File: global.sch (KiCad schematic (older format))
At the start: 37 parts, among them Q5 MMBT3904, U11 74HC165, U12 74HC595, U13 74HC595, U14 74HC595, U5 74HCT125

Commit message: added package field
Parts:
- C44, C45, C46, C50, C6, R10, R11, R34, R47, R48, R53, R56, R59, R64, R65, R67, R68, R69, R7, R70, R71, R72, R73, R74, R75, R8, R9: Package (none) -> 0603
- Q5: Package (none) -> SOT-23
- U11, U12, U13, U14: Package (none) -> SOIC-16
- U5: Package (none) -> SOIC-14
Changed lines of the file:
@@
 F 4 "Texas Instruments" H 6000 4350 50  0001 C CNN "MFN"
 F 5 "SN74HC165D" H 6000 4350 50  0001 C CNN "MFP"
+F 6 "SOIC-16" H 6000 4350 50  0001 C CNN "Package"
 	1    5500 5100
 	1    0    0    -1
@@
 F 4 "Texas Instruments" H 6000 150 50  0001 C CNN "MFN"
 F 5 "SN74HC595D" H 6000 150 50  0001 C CNN "MFP"
+F 6 "SOIC-16" H 6000 150 50  0001 C CNN "Package"
 	1    5500 900
 	1    0    0    -1
@@
 F 4 "Texas Instruments" H 6000 1550 50  0001 C CNN "MFN"
 F 5 "SN74HC595D" H 6000 1550 50  0001 C CNN "MFP"
+F 6 "SOIC-16" H 5500 2300 60  0001 C CNN "Package"
 	1    5500 2300
 	1    0    0    -1
@@
 F 4 "Texas Instruments" H 6000 2950 50  0001 C CNN "MFN"
 F 5 "SN74HC595D" H 6000 2950 50  0001 C CNN "MFP"
+F 6 "SOIC-16" H 6000 2950 50  0001 C CNN "Package"
 	1    5500 3700
 	1    0    0    -1
@@
 F 4 "Murata" H 5025 7050 50  0001 C CNN "MFN"
 F 5 "GRM188R71E104JA01J" H 5025 7050 50  0001 C CNN "MFP"
+F 6 "0603" H 5025 7050 50  0001 C CNN "Package"
 	1    5000 6850
 	1    0    0    -1
@@
 F 4 "Murata" H 5325 7050 50  0001 C CNN "MFN"
 F 5 "GRM188R71E104JA01J" H 5325 7050 50  0001 C CNN "MFP"
+F 6 "0603" H 5325 7050 50  0001 C CNN "Package"
 	1    5300 6850
 	1    0    0    -1
@@
 F 4 "Murata" H 5625 7050 50  0001 C CNN "MFN"
 F 5 "GRM188R71E104JA01J" H 5625 7050 50  0001 C CNN "MFP"
+F 6 "0603" H 5625 7050 50  0001 C CNN "Package"
 	1    5600 6850
 	1    0    0    -1
@@
 F 4 "Murata" H 5925 7050 50  0001 C CNN "MFN"
 F 5 "GRM188R71E104JA01J" H 5925 7050 50  0001 C CNN "MFP"
+F 6 "0603" H 5925 7050 50  0001 C CNN "Package"
 	1    5900 6850
 	1    0    0    -1
@@
 F 4 "Murata" H 6225 7050 50  0001 C CNN "MFN"
 F 5 "GRM188R71E104JA01J" H 6225 7050 50  0001 C CNN "MFP"
+F 6 "0603" H 6225 7050 50  0001 C CNN "Package"
 	1    6200 6850
 	1    0    0    -1
@@
 F 4 "Panasonic" H 6650 5200 50  0001 C CNN "MFN"
 F 5 "ERJ-3EKF1002V" H 6650 5200 50  0001 C CNN "MFP"
+F 6 "0603" H 6650 5200 50  0001 C CNN "Package"
 	1    6700 4950
 	1    0    0    -1
@@
 F 4 "Panasonic" H 6750 5200 50  0001 C CNN "MFN"
 F 5 "ERJ-3EKF1002V" H 6750 5200 50  0001 C CNN "MFP"
+F 6 "0603" H 6750 5200 50  0001 C CNN "Package"
 	1    6800 4950
 	1    0    0    -1
@@
 F 4 "Panasonic" H 6850 5200 50  0001 C CNN "MFN"
 F 5 "ERJ-3EKF1002V" H 6850 5200 50  0001 C CNN "MFP"
+F 6 "0603" H 6850 5200 50  0001 C CNN "Package"
 	1    6900 4950
 	1    0    0    -1
@@
 F 4 "Panasonic" H 6950 5200 50  0001 C CNN "MFN"
 F 5 "ERJ-3EKF1002V" H 6950 5200 50  0001 C CNN "MFP"
+F 6 "0603" H 6950 5200 50  0001 C CNN "Package"
 	1    7000 4950
 	1    0    0    -1
@@
 F 4 "Panasonic" H 7050 5200 50  0001 C CNN "MFN"
 F 5 "ERJ-3EKF1002V" H 7050 5200 50  0001 C CNN "MFP"
+F 6 "0603" H 7050 5200 50  0001 C CNN "Package"
 	1    7100 4950
 	1    0    0    -1
@@
 F 4 "Panasonic" H 6700 2650 50  0001 C CNN "MFN"
 F 5 "ERJ-3EKF1001V" H 6700 2650 50  0001 C CNN "MFP"
+F 6 "0603" H 6700 2650 50  0001 C CNN "Package"
 	1    6750 2400
 	0    1    1    0
@@
 F 4 "Panasonic" H 6700 2550 50  0001 C CNN "MFN"
 F 5 "ERJ-3EKF1001V" H 6700 2550 50  0001 C CNN "MFP"
+F 6 "0603" H 6700 2550 50  0001 C CNN "Package"
 	1    6750 2300
 	0    1    1    0
@@
 F 4 "Panasonic" H 6700 2750 50  0001 C CNN "MFN"
 F 5 "ERJ-3EKF1001V" H 6700 2750 50  0001 C CNN "MFP"
+F 6 "0603" H 6700 2750 50  0001 C CNN "Package"
 	1    6750 2500
 	0    1    1    0
@@
 F 4 "Panasonic" H 6700 2850 50  0001 C CNN "MFN"
 F 5 "ERJ-3EKF1001V" H 6700 2850 50  0001 C CNN "MFP"
+F 6 "0603" H 6700 2850 50  0001 C CNN "Package"
 	1    6750 2600
 	0    1    1    0
@@
 F 4 "Panasonic" H 6700 3250 50  0001 C CNN "MFN"
 F 5 "ERJ-3EKF1001V" H 6700 3250 50  0001 C CNN "MFP"
+F 6 "0603" H 6700 3250 50  0001 C CNN "Package"
 	1    6750 3000
 	0    1    1    0
@@
 F 4 "Panasonic" H 6700 3150 50  0001 C CNN "MFN"
 F 5 "ERJ-3EKF1001V" H 6700 3150 50  0001 C CNN "MFP"
+F 6 "0603" H 6700 3150 50  0001 C CNN "Package"
 	1    6750 2900
 	0    1    1    0
@@
 F 4 "Panasonic" H 6700 3050 50  0001 C CNN "MFN"
 F 5 "ERJ-3EKF1001V" H 6700 3050 50  0001 C CNN "MFP"
+F 6 "0603" H 6700 3050 50  0001 C CNN "Package"
 	1    6750 2800
 	0    1    1    0
@@
 F 4 "Panasonic" H 6700 2950 50  0001 C CNN "MFN"
 F 5 "ERJ-3EKF1001V" H 6700 2950 50  0001 C CNN "MFP"
+F 6 "0603" H 6700 2950 50  0001 C CNN "Package"
 	1    6750 2700
 	0    1    1    0
@@
 F 4 "Texas Instruments" H 3000 800 60  0001 C CNN "MFN"
 F 5 "SN74HCT125D" H 3000 800 60  0001 C CNN "MFP"
+F 6 "SOIC-14" H 3500 -150 50  0001 C CNN "Package"
 	1    3000 800
 	1    0    0    -1
@@
 F 4 "Panasonic" H 8980 1150 50  0001 C CNN "MFN"
 F 5 "ERJ-3EKF3302V" H 8980 1150 50  0001 C CNN "MFP"
+F 6 "0603" H 8980 1150 50  0001 C CNN "Package"
 	1    8900 1050
 	-1   0    0    1
@@
 F 4 "Panasonic" H 8980 2350 50  0001 C CNN "MFN"
 F 5 "ERJ-3EKF1004V" H 8980 2350 50  0001 C CNN "MFP"
+F 6 "0603" H 8980 2350 50  0001 C CNN "Package"
 	1    8900 2250
 	-1   0    0    1
@@
 F 4 "Panasonic" H 8380 1150 50  0001 C CNN "MFN"
 F 5 "ERJ-3EKF3302V" H 8380 1150 50  0001 C CNN "MFP"
+F 6 "0603" H 8380 1150 50  0001 C CNN "Package"
 	1    8300 1050
 	-1   0    0    1
@@
 F 4 "Panasonic" H 8580 1150 50  0001 C CNN "MFN"
 F 5 "ERJ-3EKF3302V" H 8580 1150 50  0001 C CNN "MFP"
+F 6 "0603" H 8580 1150 50  0001 C CNN "Package"
 	1    8500 1050
 	-1   0    0    1
@@
 F 4 "Panasonic" H 8780 1150 50  0001 C CNN "MFN"
 F 5 "ERJ-3EKF3302V" H 8780 1150 50  0001 C CNN "MFP"
+F 6 "0603" H 8780 1150 50  0001 C CNN "Package"
 	1    8700 1050
 	-1   0    0    1
@@
 F 4 "Panasonic" H 2780 5750 50  0001 C CNN "MFN"
 F 5 "ERJ-3EKF1002V" H 2780 5750 50  0001 C CNN "MFP"
+F 6 "0603" H 2780 5750 50  0001 C CNN "Package"
 	1    2700 5650
 	1    0    0    -1
@@
 F 4 "ON Semiconductor" H 4200 2875 50  0001 C CNN "MFN"
 F 5 "MMBT3904LT1G" H 4200 2875 50  0001 C CNN "MFP"
+F 6 "SOT-23" H 4200 2875 50  0001 C CNN "Package"
 	1    4000 2700
 	1    0    0    -1
@@
 F 4 "Panasonic" H 4180 2250 50  0001 C CNN "MFN"
 F 5 "ERJ-3EKF1002V" H 4180 2250 50  0001 C CNN "MFP"
+F 6 "0603" H 4180 2250 50  0001 C CNN "Package"
 	1    4100 2150
 	1    0    0    -1
@@
 F 4 "Panasonic" H 3530 2800 50  0001 C CNN "MFN"
 F 5 "ERJ-3EKF1002V" H 3530 2800 50  0001 C CNN "MFP"
+F 6 "0603" H 3530 2800 50  0001 C CNN "Package"
 	1    3450 2700
 	0    1    1    0
@@
 F 4 "Panasonic" H 3780 3050 50  0001 C CNN "MFN"
 F 5 "ERJ-3EKF1003V" H 3780 3050 50  0001 C CNN "MFP"
+F 6 "0603" H 3780 3050 50  0001 C CNN "Package"
 	1    3700 2950
 	1    0    0    -1

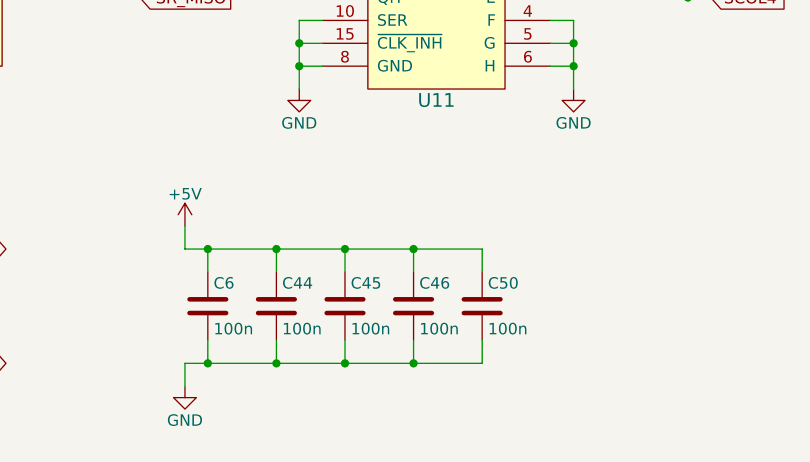
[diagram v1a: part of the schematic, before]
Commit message: renumbered components
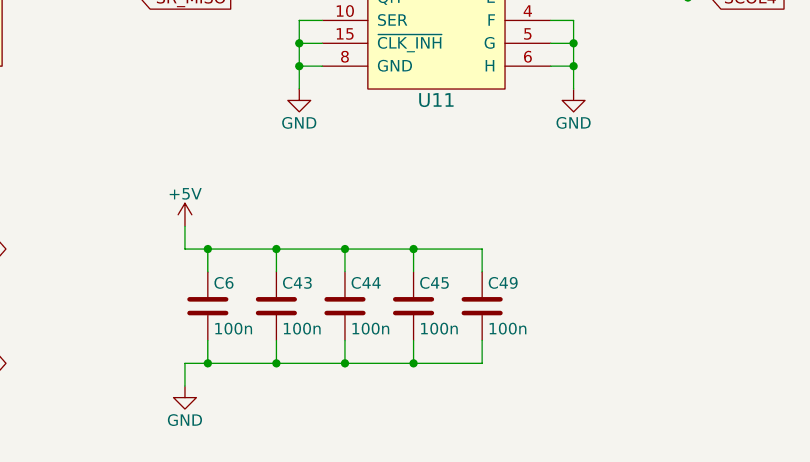
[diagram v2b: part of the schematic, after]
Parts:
- renumbered C44 to C43, C45 to C44, C46 to C45, C50 to C49
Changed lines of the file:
@@
 $EndComp
 $Comp
-L C C44
+L C C43
 U 1 1 59DAD399
 P 5300 6850
-F 0 "C44" H 5325 6950 50  0000 L CNN
+F 0 "C43" H 5325 6950 50  0000 L CNN
 F 1 "100n" H 5325 6750 50  0000 L CNN
 F 2 "w_capacitor:C_0603" H 5338 6700 50  0001 C CNN
@@
 $EndComp
 $Comp
-L C C45
+L C C44
 U 1 1 59DAD3D5
 P 5600 6850
-F 0 "C45" H 5625 6950 50  0000 L CNN
+F 0 "C44" H 5625 6950 50  0000 L CNN
 F 1 "100n" H 5625 6750 50  0000 L CNN
 F 2 "w_capacitor:C_0603" H 5638 6700 50  0001 C CNN
@@
 $EndComp
 $Comp
-L C C46
+L C C45
 U 1 1 59DAD3DB
 P 5900 6850
-F 0 "C46" H 5925 6950 50  0000 L CNN
+F 0 "C45" H 5925 6950 50  0000 L CNN
 F 1 "100n" H 5925 6750 50  0000 L CNN
 F 2 "w_capacitor:C_0603" H 5938 6700 50  0001 C CNN
@@
 $EndComp
 $Comp
-L C C50
+L C C49
 U 1 1 59DB526D
 P 6200 6850
-F 0 "C50" H 6225 6950 50  0000 L CNN
+F 0 "C49" H 6225 6950 50  0000 L CNN
 F 1 "100n" H 6225 6750 50  0000 L CNN
 F 2 "w_capacitor:C_0603" H 6238 6700 50  0001 C CNN

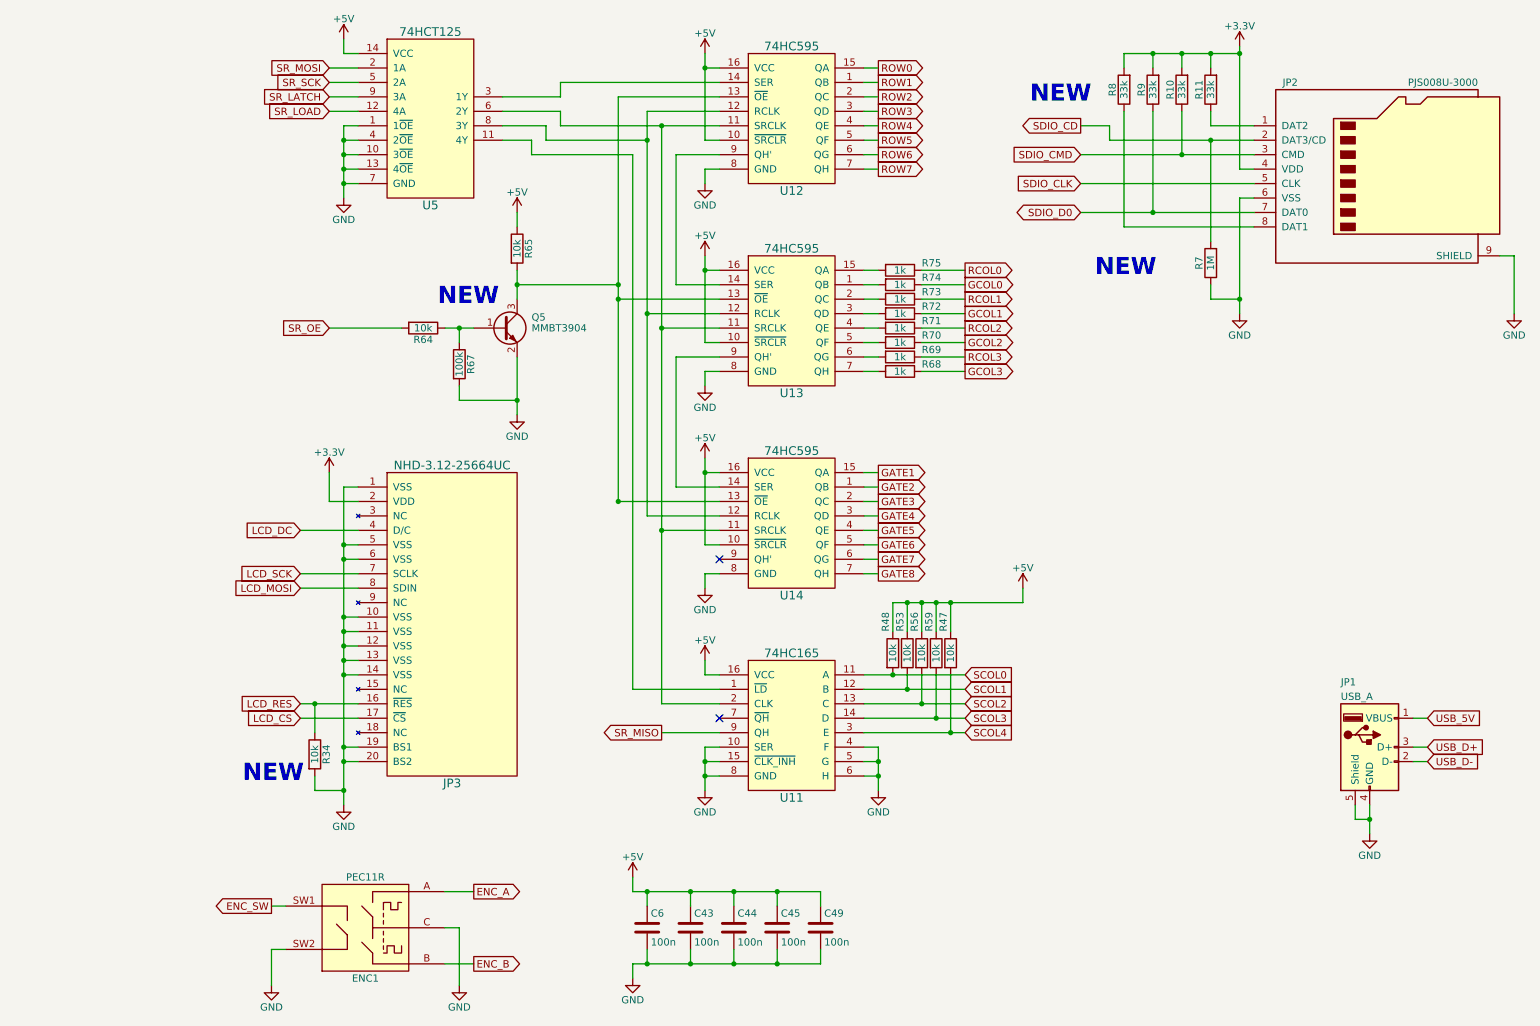
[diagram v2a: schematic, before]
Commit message: cleanup schematics and updated to revision 0.3
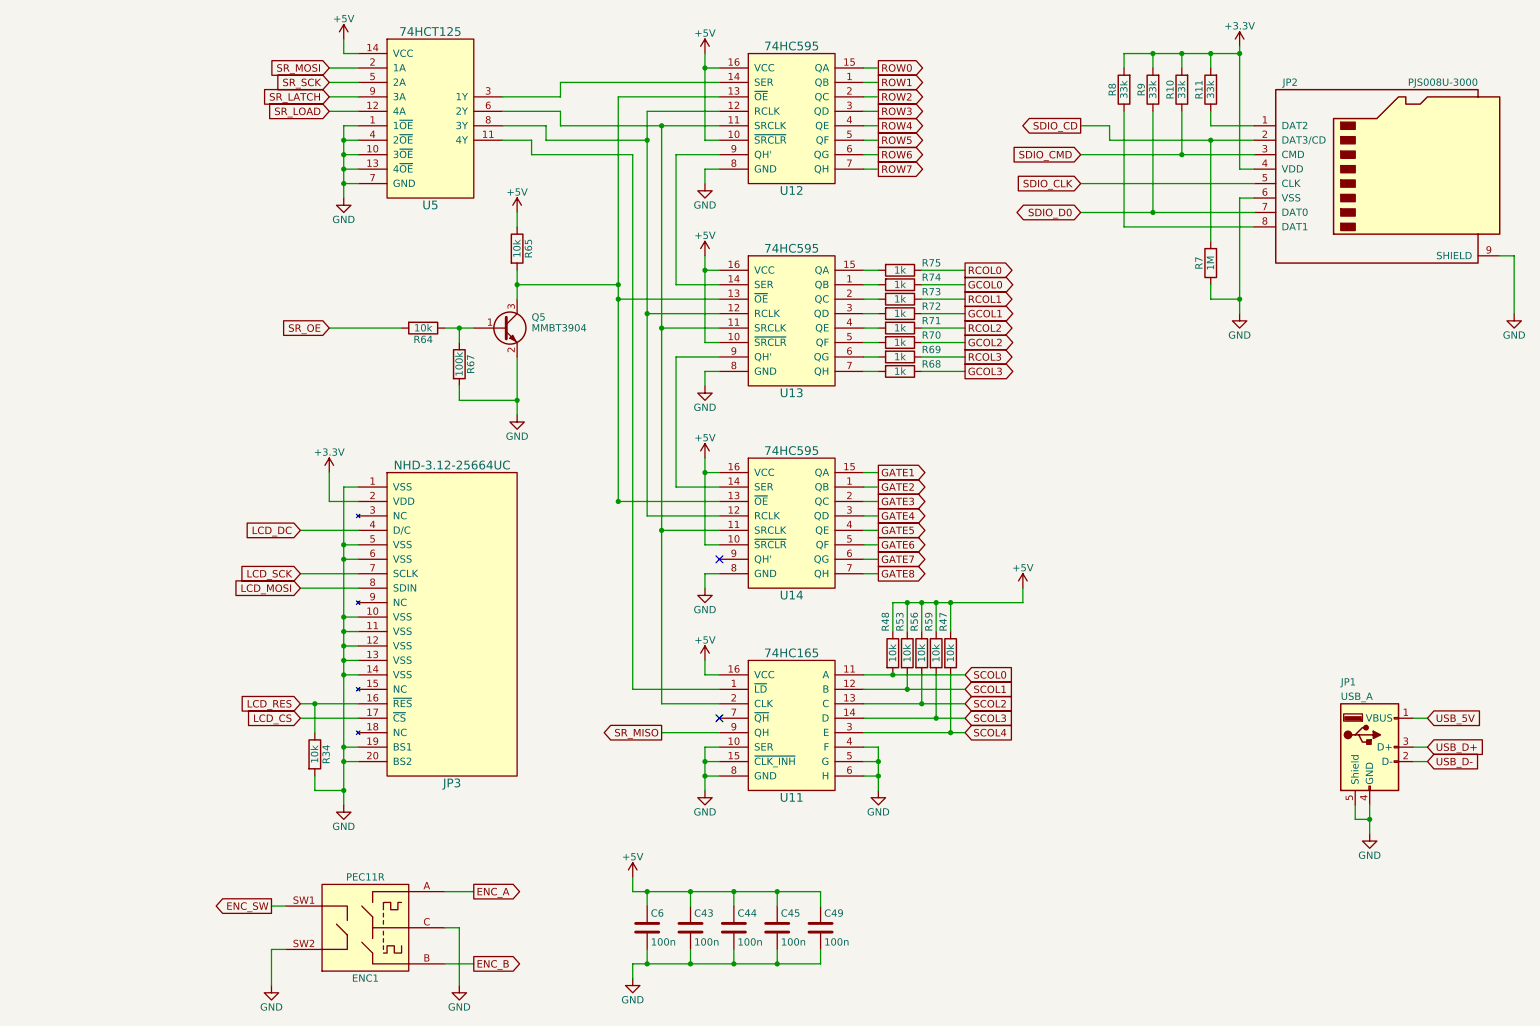
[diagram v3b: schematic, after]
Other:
- note removed: "NEW"
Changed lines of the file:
@@
 Sheet 2 8
 Title "per|former eurorack sequencer"
-Date ""
-Rev "0.2"
+Date "2018-08-26"
+Rev "0.3"
 Comp "westlicht"
 Comment1 "cc-by-sa"
@@
 Text GLabel 2800 2700 0    51   Input ~ 0
 SR_OE
-Text Notes 8100 2350 0    118  ~ 24
-NEW
-Text Notes 3550 2550 0    118  ~ 24
-NEW
-Text Notes 2200 5850 0    118  ~ 24
-NEW
-Text Notes 7650 1150 0    118  ~ 24
-NEW
 Wire Wire Line
 	6500 900  6600 900

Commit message: cleaned up schematics
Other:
- note added: "BUTTON / LED MATRIX DRIVER"
- note added: "ENCODER"
- note added: "OLED DISPLAY"
- note added: "SD CARD"
- note added: "USB PORT"
- moved on the sheet: C43, C44, C45, C49, C6, ENC1, JP1, JP2, JP3, Q5, R10, R11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
